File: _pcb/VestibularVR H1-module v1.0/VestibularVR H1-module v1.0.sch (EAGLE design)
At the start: 70 parts, among them IC1 FT232RL, IC2 74LVC1G07DBV, IC3 TLV70033DDCR, IC4 74LVC1G07DBV, IC5 74LVC1G07DBV, IC6 74LVC1G07DBV, IC7 USBLC6-2SC6, IC8 ATXMEGA32A4U, X1 TSW-105-02-S-D, X2 TSW-105-02-S-D, X7 22-23-2051

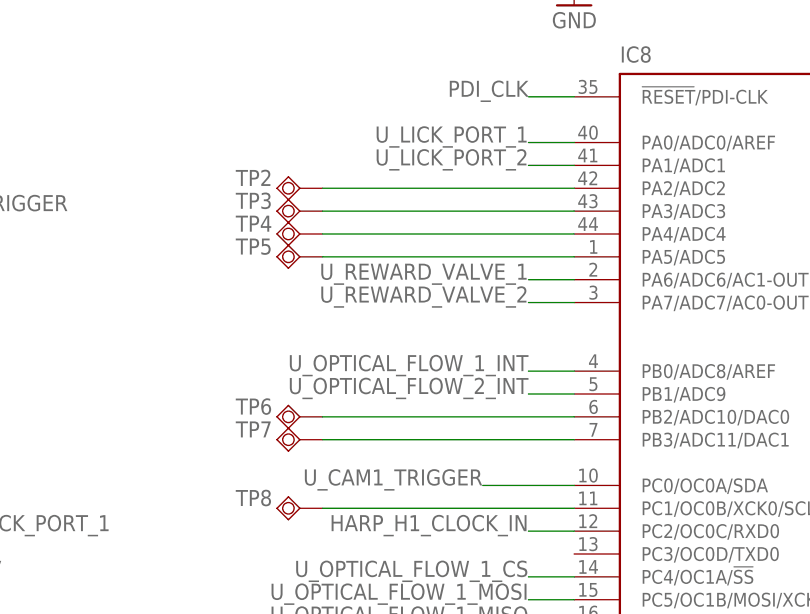
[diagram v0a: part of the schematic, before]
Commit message: v.1.0 pcb design as finished; still missing to hear about it from Filipe
. David's pcb v.1.0 design as finished
  - mechanical holes final tuning
  - main labels final design
. still missing to hear about it from Filipe
. next step - building BOM
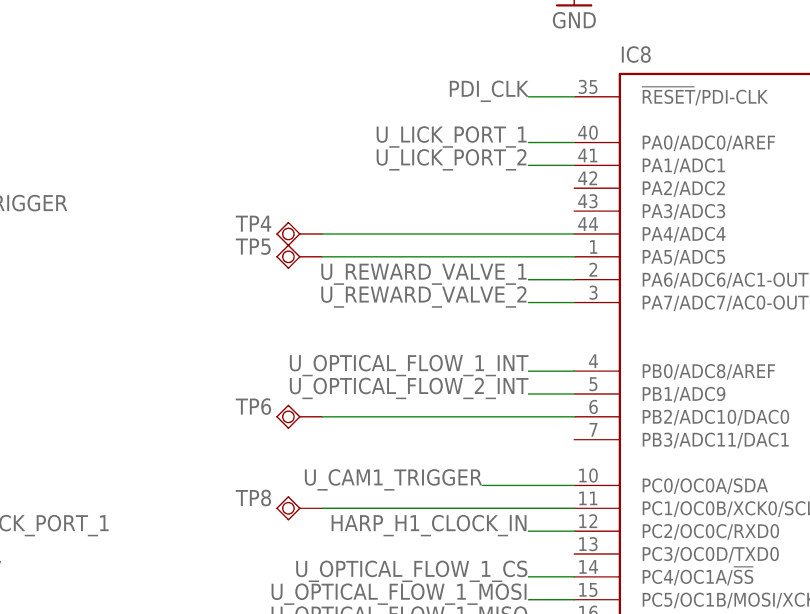
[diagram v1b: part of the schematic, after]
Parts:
- removed TP2, TP3, TP7: WIREPADSMD1,27-254, testpad:TPSQTP11R
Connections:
- removed net N$10: IC8.PA3/ADC3, TP3.TP
- removed net N$15: IC8.PB3/ADC11/DAC1, TP7.TP
- removed net N$8: IC8.PA2/ADC2, TP2.TP
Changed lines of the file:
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@@
 <attribute name="DIGKEYPN" value=""/>
 </part>
-<part name="TP2" library="testpad" library_urn="urn:adsk.eagle:library:385" deviceset="TPSQ" device="TP11R" package3d_urn="urn:adsk.eagle:package:27961/1" value="WIREPADSMD1,27-254"/>
-<part name="TP3" library="testpad" library_urn="urn:adsk.eagle:library:385" deviceset="TPSQ" device="TP11R" package3d_urn="urn:adsk.eagle:package:27961/1" value="WIREPADSMD1,27-254"/>
 <part name="TP4" library="testpad" library_urn="urn:adsk.eagle:library:385" deviceset="TPSQ" device="TP11R" package3d_urn="urn:adsk.eagle:package:27961/1" value="WIREPADSMD1,27-254"/>
 <part name="TP5" library="testpad" library_urn="urn:adsk.eagle:library:385" deviceset="TPSQ" device="TP11R" package3d_urn="urn:adsk.eagle:package:27961/1" value="WIREPADSMD1,27-254"/>
 <part name="TP6" library="testpad" library_urn="urn:adsk.eagle:library:385" deviceset="TPSQ" device="TP11R" package3d_urn="urn:adsk.eagle:package:27961/1" value="WIREPADSMD1,27-254"/>
-<part name="TP7" library="testpad" library_urn="urn:adsk.eagle:library:385" deviceset="TPSQ" device="TP11R" package3d_urn="urn:adsk.eagle:package:27961/1" value="WIREPADSMD1,27-254"/>
 <part name="TP8" library="testpad" library_urn="urn:adsk.eagle:library:385" deviceset="TPSQ" device="TP11R" package3d_urn="urn:adsk.eagle:package:27961/1" value="WIREPADSMD1,27-254"/>
 <part name="TP9" library="testpad" library_urn="urn:adsk.eagle:library:385" deviceset="TPSQ" device="TP11R" package3d_urn="urn:adsk.eagle:package:27961/1" value="WIREPADSMD1,27-254"/>
@@
 <attribute name="DIGKEYPN" x="67.31" y="121.92" size="1.778" layer="96" rot="MR0" display="off"/>
 </instance>
-<instance part="TP2" gate="G$1" x="124.46" y="187.96" smashed="yes" rot="R270">
-<attribute name="NAME" x="117.348" y="188.214" size="1.778" layer="95"/>
-</instance>
-<instance part="TP3" gate="G$1" x="124.46" y="185.42" smashed="yes" rot="R270">
-<attribute name="NAME" x="117.348" y="185.674" size="1.778" layer="95"/>
-</instance>
 <instance part="TP4" gate="G$1" x="124.46" y="182.88" smashed="yes" rot="R270">
 <attribute name="NAME" x="117.348" y="183.134" size="1.778" layer="95"/>
@@
 <instance part="TP6" gate="G$1" x="124.46" y="162.56" smashed="yes" rot="R270">
 <attribute name="NAME" x="117.348" y="162.814" size="1.778" layer="95"/>
-</instance>
-<instance part="TP7" gate="G$1" x="124.46" y="160.02" smashed="yes" rot="R270">
-<attribute name="NAME" x="117.348" y="160.274" size="1.778" layer="95"/>
 </instance>
 <instance part="TP8" gate="G$1" x="124.46" y="152.4" smashed="yes" rot="R270">
@@
 </segment>
 </net>
-<net name="N$8" class="0">
-<segment>
-<pinref part="IC8" gate="G$1" pin="PA2/ADC2"/>
-<pinref part="TP2" gate="G$1" pin="TP"/>
-<wire x1="154.94" y1="187.96" x2="127" y2="187.96" width="0.1524" layer="91"/>
-</segment>
-</net>
-<net name="N$10" class="0">
-<segment>
-<pinref part="TP3" gate="G$1" pin="TP"/>
-<pinref part="IC8" gate="G$1" pin="PA3/ADC3"/>
-<wire x1="127" y1="185.42" x2="154.94" y2="185.42" width="0.1524" layer="91"/>
-</segment>
-</net>
 <net name="N$11" class="0">
 <segment>
@@
 </segment>
 </net>
-<net name="N$15" class="0">
-<segment>
-<pinref part="IC8" gate="G$1" pin="PB3/ADC11/DAC1"/>
-<pinref part="TP7" gate="G$1" pin="TP"/>
-<wire x1="154.94" y1="160.02" x2="127" y2="160.02" width="0.1524" layer="91"/>
-</segment>
-</net>

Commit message: final versions committed & CAM data
VestibularVR H1-module v1.0
  &
Lick Sensor module v1.0
final versions committed !!!

.created CAM data for both boards
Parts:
- removed CAMM_TRIGGER: 22-23-2041, con-molex:22-23-2041
- removed X7: 22-23-2051, con-molex:22-23-2051
- added CAM_TRIGGERS: 22-23-2041, con-molex:22-23-2041
- added X15: (no value), con-weidmueller-sl35:90G-5
- L1, L2: device rcl:R-EU_R0805 -> rcl:R-EU_R0603
- renumbered LICK_PORT_1 to LICK_0, LICK_PORT_2 to LICK_1, REWARD_VALVE to VALVES, U$1 to X3, U$2 to OSC1, U$4 to T2, U$7 to T1
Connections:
- removed net N$16: CAMM_TRIGGER-4.S, IC2.Y
- removed net N$59: C2.1, X3.P$4
- new net N$15: C2.1, X3.P$3
- new net N$8: CAM_TRIGGERS-2.S, IC4.Y
- net +12V: now also X15.1; no longer X7-5.S
- net GND: now also CAM_TRIGGERS-1.S, CAM_TRIGGERS-3.S, X15.5; no longer CAMM_TRIGGER-1.S, CAMM_TRIGGER-3.S, X7-1.S
- net HARP_H1_BOARD_RX: now also X15.3; no longer X7-3.S
- net HARP_H1_BOARD_TX: now also X15.2; no longer X7-4.S
- net HARP_H1_CLOCK_IN: now also X15.4; no longer X7-2.S
- net N$1: now also X3.P$2; no longer X3.P$1
- net N$4: now also CAM_TRIGGERS-4.S, IC2.Y; no longer CAMM_TRIGGER-2.S, IC4.Y
- net U_CAM1_TRIGGER: now also IC4.A; no longer IC2.A
- net U_CAM2_TRIGGER: now also IC2.A; no longer IC4.A
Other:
- note removed: "a reverificar: - pinos CTS RTS: correctos com refª q o Filipe disse? - u_CAM_x trigger em pinos PD0 & PB0; interrupts level; Certo? - HARP_HQ_CLOCK_IN em PC": OK? - u_OPTICAL_FLOW_1_INT: verificar os pinos"
- moved on the sheet: C15, C16, C2, IC2, IC4, R1, R2, R5, R6

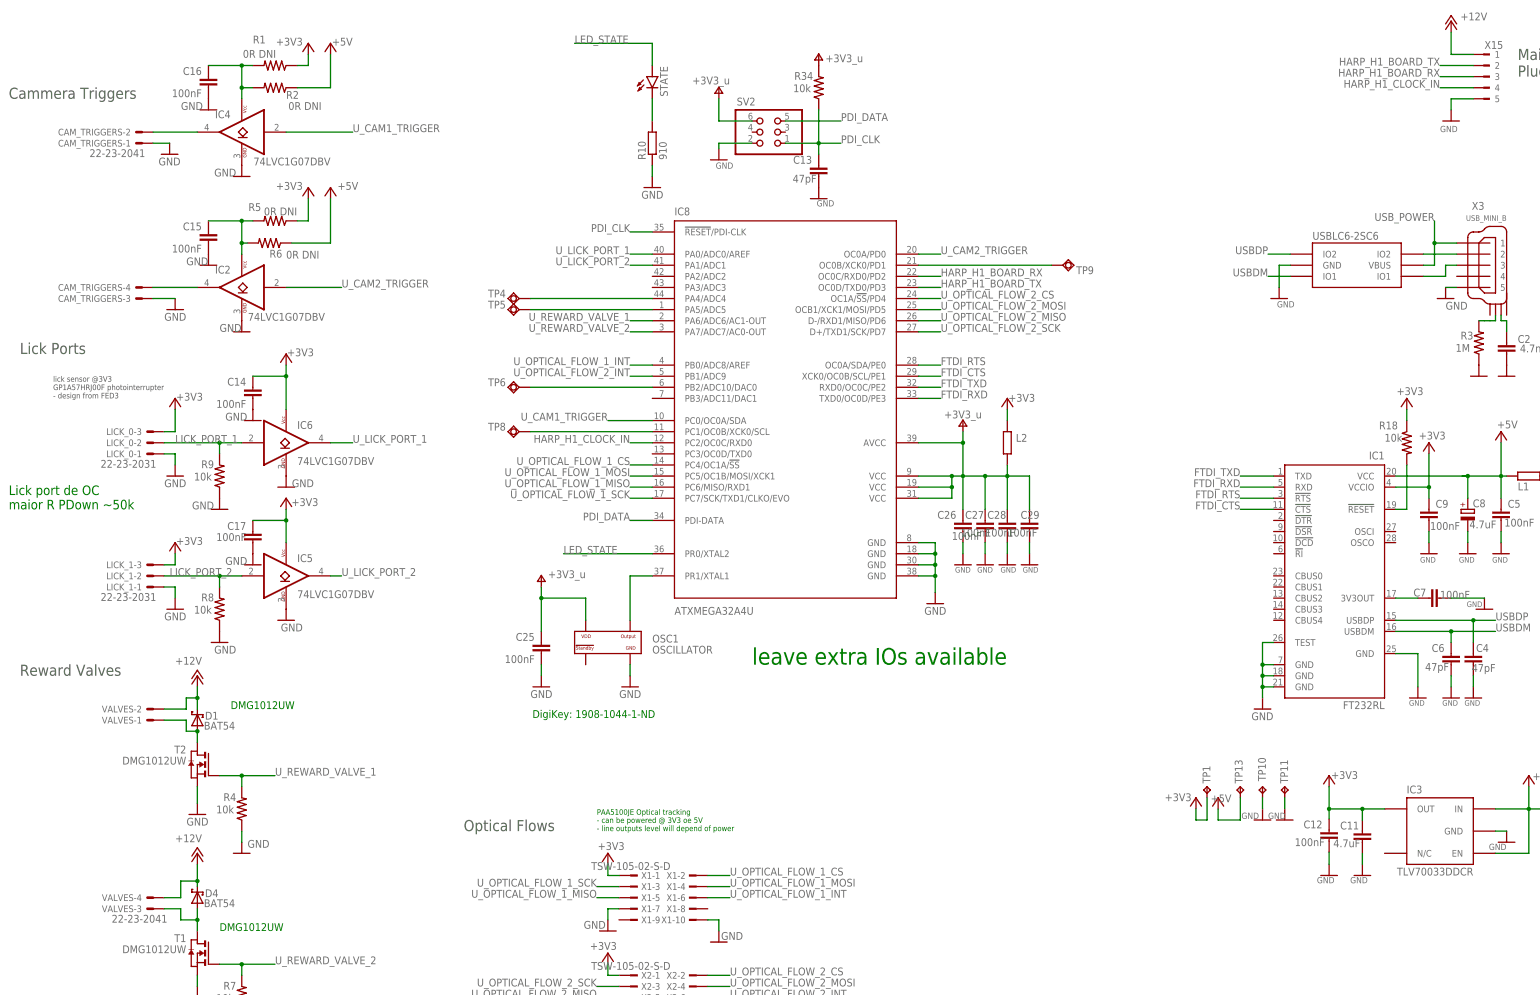
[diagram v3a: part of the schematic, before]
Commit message: BOMs building
. BOMs building:
  - for both projects - Lick Sensor Module v1.0 & VestibularVR H1 Module v1.0
  - schm files modified (components parameters updated)

. Removed old Auxiliary Designs
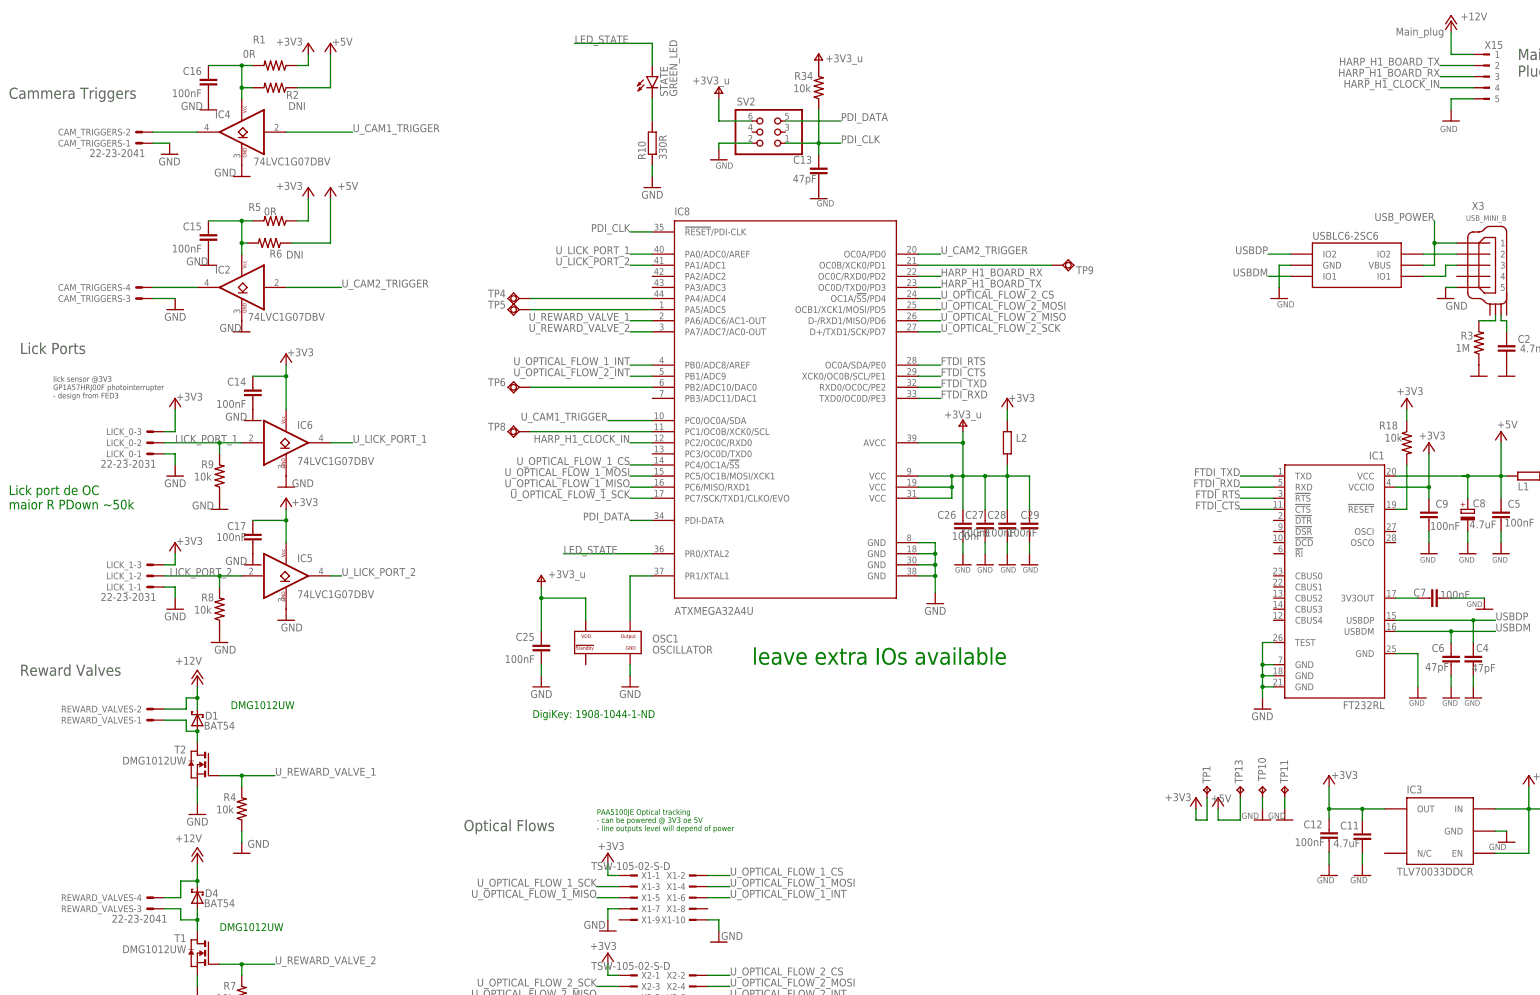
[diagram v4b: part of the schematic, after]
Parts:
- C12: DIGIKEY_PN (none) -> 445-5932-1-ND; MPN MC0402B104K160CT -> C1005X7R1H104K050BB
- C3, C9: device rcl:C-EUC0402 -> rcl:C-EUC0402K; DIGIKEY_PN (none) -> 445-5932-1-ND; MPN MC0402B104K160CT -> C1005X7R1H104K050BB; NOTES (none) -> -; TYPE (none) -> SMD
- C5, C7: DIGIKEY_PN (none) -> 445-5932-1-ND; MPN MC0402B104K160CT -> C1005X7R1H104K050BB; NOTES (none) -> -; TYPE (none) -> SMD
- R1, R5: value 0R DNI -> 0R
- R10: value 910 -> 330R
- R18: DIGIKEY_PN (none) -> 541-3959-1-ND; NOTES (none) -> -; TYPE (none) -> SMD
- R2, R6: value 0R DNI -> DNI
- STATE: value (none) -> GREEN_LED
- TP1, TP10, TP11, TP13: value TPB1,27 -> NO_COMPONENT
- TP4, TP5, TP6, TP8, TP9: value WIREPADSMD1,27-254 -> NO_COMPONENT
- X15: value (none) -> Main_plug
- renumbered VALVES to REWARD_VALVES

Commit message: BOM files
BOM files
- Lick sensor module v1.0 BOM; NOT FINAL
VESTIBULARVR H1 v.1.0: added schm notes
- VESTIBULARVR H1 v.1.0 BOM; NOT FINAL
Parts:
- OSC1: MPN (none) -> DSC1001CI5-032.0000; OEPS_PN (none) -> OEPS080018
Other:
- note added: "-to review USBDP & USBDP pin switched!!!"
- note removed: "DigiKey: 1908-1044-1-ND"
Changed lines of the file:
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@@
 <part name="R5" library="rcl" library_urn="urn:adsk.eagle:library:334" deviceset="R-US_" device="R0402" package3d_urn="urn:adsk.eagle:package:23547@1/3" value="0R"/>
 <part name="R6" library="rcl" library_urn="urn:adsk.eagle:library:334" deviceset="R-US_" device="R0402" package3d_urn="urn:adsk.eagle:package:23547@1/3" value="DNI"/>
-<part name="OSC1" library="VestibularVR H1-module v1.0" deviceset="OSCILLATOR" device=""/>
+<part name="OSC1" library="VestibularVR H1-module v1.0" deviceset="OSCILLATOR" device="">
+<attribute name="MPN" value="DSC1001CI5-032.0000"/>
+<attribute name="OEPS_PN" value="OEPS080018"/>
+</part>
 <part name="R4" library="rcl" library_urn="urn:adsk.eagle:library:334" deviceset="R-US_" device="R0402" package3d_urn="urn:adsk.eagle:package:23547@1/3" value="10k">
 <attribute name="DIGIKEY_PN" value="541-3959-1-ND"/>
@@
 - design from FED3
 </text>
-<text x="127.508" y="86.868" size="1.778" layer="91">DigiKey: 1908-1044-1-ND</text>
 <text x="177.8" y="99.06" size="3.81" layer="91" font="vector" ratio="20" distance="2">leave extra IOs available
 </text>
@@
 <text x="58.42" y="88.9" size="1.778" layer="91">DMG1012UW</text>
 <text x="55.88" y="38.1" size="1.778" layer="91">DMG1012UW</text>
+<text x="266.7" y="185.42" size="2.54" layer="91" font="vector" ratio="16">-to review
+  USBDP &amp; USBDP pin switched!!!</text>
 </plain>
 <instances>
@@
 <attribute name="VALUE" x="154.94" y="101.6" size="1.778" layer="96"/>
 <attribute name="NAME" x="154.94" y="104.14" size="1.778" layer="95"/>
+<attribute name="OEPS_PN" x="144.78" y="104.14" size="1.778" layer="96" display="off"/>
+<attribute name="MPN" x="144.78" y="104.14" size="1.778" layer="96" display="off"/>
 </instance>
 <instance part="R4" gate="G$1" x="60.96" y="66.04" smashed="yes" rot="R90">

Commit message: BOM being updated
BOM being updated
not yet finished
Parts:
- C10, C11: OEPS (none) -> OEPS010018
- C12, C14, C15, C16, C17, C25, C26, C27, C28, C29, C3, C5, C7, C9: OEPS (none) -> OEPS010004
- C13, C4, C6: OEPS (none) -> OEPS080013
- C2: MPN 04025C472KAT2A -> CC0402KRX7R8BB472; OEPS (none) -> OEPS010001
- C8: device rcl:CPOL-EUA/3216-18R -> rcl:C-EUC0603; MPN TAJA475K010 -> C1608X6S1C475K080AC; OEPS (none) -> OEPS010018
- CAM_TRIGGERS, REWARD_VALVES: OEPS (none) -> N.A.1
- D1, D4: MPN (none) -> BAT54SLT1G; OEPS (none) -> OEPS030003
- IC1: MPN (none) -> FT232RL; OEPS (none) -> OEPS080013
- IC2, IC4, IC5, IC6: MPN (none) -> SN74LVC1G07DBVR; OEPS (none) -> n.a.
- IC3: value TLV70033DDCR -> LP5907MFX-3.3; MPN TLV70033DDCR -> LP5907MFX-3.3/NOPB; OEPS (none) -> OEPS080016
- IC7: MPN (none) -> USBLC6-2SC6; OEPS (none) -> OEPS030010
- IC8: OEPS (none) -> OEPS080012
- L1, L2: OEPS (none) -> OEPS040003
- LICK_0, LICK_1: OEPS (none) -> N.A.2
- OSC1: OEPS (none) -> OEPS080018; OEPS_PN OEPS080018 -> (none)
- R1, R5: MPN (none) -> RC0402JR-070RL; OEPS (none) -> OEPS020001
- R10: MPN (none) -> RC0402FR-07330RL; OEPS (none) -> OEPS020037
- R18, R34: NOTES - -> (none); OEPS (none) -> OEPS020030; TYPE SMD -> (none)
- R2, R6: MPN (none) -> DNI; OEPS (none) -> DNI
- R3: DIGIKEY_PN (none) -> 541-1.00MLCT-ND; MPN (none) -> CRCW04021M00FKED; OEPS (none) -> OEPS020026; PN CRCW04021M00FKED -> (none)
- R4, R7: DIGIKEY_PN 541-3959-1-ND -> 541-10.0KLCT-ND; NOTES - -> (none); OEPS (none) -> OEPS020030; TYPE SMD -> (none)
- R8, R9: value 10k -> 1M; DIGIKEY_PN 541-3959-1-ND -> 541-1.00MLCT-ND; MPN CRCW040210K0FKED -> CRCW04021M00FKED; NOTES - -> (none); OEPS (none) -> OEPS020026; TYPE SMD -> (none)
- STATE: MPN (none) -> LTST-C191KGKT; OEPS (none) -> OEPS030005
- SV2: MPN (none) -> 609-3210-ND; OEPS (none) -> OEPS070015
- T1, T2: MPN (none) -> DMG1012UW-7; OEPS (none) -> OEPS060010
- X1, X2: MPN (none) -> 2x5 header; OEPS (none) -> n.a.
- X15: MPN (none) -> 20.155MH/5-E; OEPS (none) -> n.a.
- X3: MPN (none) -> UX60-MB-5S8; OEPS (none) -> OEPS070021
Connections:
- net +5V: now also C8.1; no longer C8.+
- net GND: now also C8.2; no longer C8.-
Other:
- note added: "-to review pinout upside-down!!!"
- note added: "PAA5100JE Optical tracking - can be powered @ 3V3 or 5V - line outputs level will depend of power"
- note removed: "PAA5100JE Optical tracking - can be powered @ 3V3 oe 5V - line outputs level will depend of power"
- note removed: "leave extra IOs available"
